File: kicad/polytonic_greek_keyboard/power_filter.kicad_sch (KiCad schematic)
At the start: 6 parts

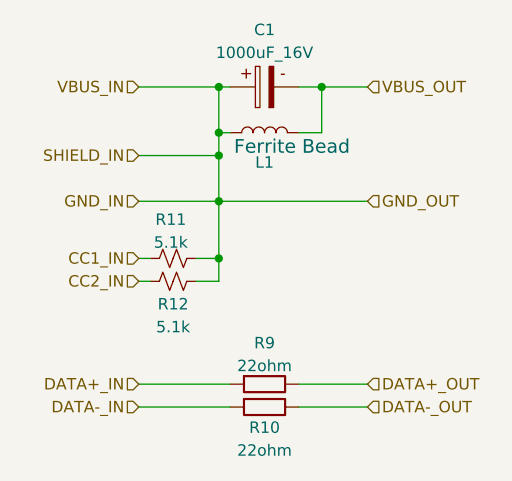
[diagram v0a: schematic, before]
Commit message: [ADD] a more structured approach of the pcb in a way that won't overload the esp32 that is running it
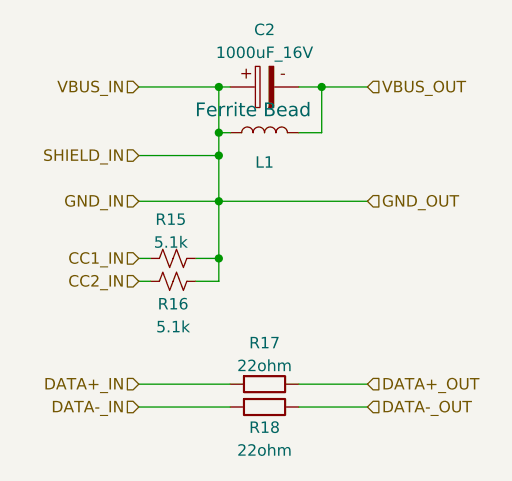
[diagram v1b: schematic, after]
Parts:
- L1: footprint Inductor_SMD:L_6.3x6.3_H3 -> Inductor_SMD:L_0201_0603Metric
- renumbered C1 to C2, R11 to R15, R12 to R16, R9 to R17, R10 to R18
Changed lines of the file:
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@@
 		(on_board yes)
 		(dnp no)
-		(property "Reference" "R10"
+		(property "Reference" "R18"
 			(at 38.1 58.166 0)
 			(effects
@@
 			)
 		)
-		(property "Description" "22Ω, 1/4W Resistor"
+		(property "Description" "20kΩ, 1/4W Resistor"
 			(at 38.1 55.88 0)
 			(effects
@@
 			(project "polytonic_greek_keyboard"
 				(path "/cbe25a1b-6c02-43c2-9ff9-ba274c7cf6a2/603682d4-9510-4466-84d6-fe473c47d1f7"
-					(reference "R10")
+					(reference "R18")
 					(unit 1)
 				)
@@
 		(on_board yes)
 		(dnp no)
-		(property "Reference" "R11"
+		(property "Reference" "R15"
 			(at 27.686 35.052 0)
 			(effects
@@
 			(project ""
 				(path "/cbe25a1b-6c02-43c2-9ff9-ba274c7cf6a2/603682d4-9510-4466-84d6-fe473c47d1f7"
-					(reference "R11")
+					(reference "R15")
 					(unit 1)
 				)
@@
 			)
 		)
-		(property "Footprint" "Inductor_SMD:L_6.3x6.3_H3"
+		(property "Footprint" "Inductor_SMD:L_0201_0603Metric"
 			(at 38.1 25.4 0)
 			(effects
@@
 		)
 		(property "Display" "Ferrite Bead"
-			(at 41.148 26.924 90)
+			(at 36.83 22.86 90)
 			(effects
 				(font
@@
 		(on_board yes)
 		(dnp no)
-		(property "Reference" "C1"
+		(property "Reference" "C2"
 			(at 38.1 13.97 0)
 			(effects
@@
 			(project ""
 				(path "/cbe25a1b-6c02-43c2-9ff9-ba274c7cf6a2/603682d4-9510-4466-84d6-fe473c47d1f7"
-					(reference "C1")
+					(reference "C2")
 					(unit 1)
 				)
@@
 		(on_board yes)
 		(dnp no)
-		(property "Reference" "R12"
+		(property "Reference" "R16"
 			(at 27.94 44.45 0)
 			(effects
@@
 			(project "polytonic_greek_keyboard"
 				(path "/cbe25a1b-6c02-43c2-9ff9-ba274c7cf6a2/603682d4-9510-4466-84d6-fe473c47d1f7"
-					(reference "R12")
+					(reference "R16")
 					(unit 1)
 				)
@@
 		(on_board yes)
 		(dnp no)
-		(property "Reference" "R9"
+		(property "Reference" "R17"
 			(at 38.1 48.768 0)
 			(effects
@@
 			)
 		)
-		(property "Description" "22Ω, 1/4W Resistor"
+		(property "Description" "20kΩ, 1/4W Resistor"
 			(at 38.1 53.34 0)
 			(effects
@@
 			(project ""
 				(path "/cbe25a1b-6c02-43c2-9ff9-ba274c7cf6a2/603682d4-9510-4466-84d6-fe473c47d1f7"
-					(reference "R9")
-					(unit 1)
-				)
+					(reference "R17")
+					(unit 1)
+				)

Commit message: [UPDATE] the board desing, [FIX] connection issues
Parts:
- L1: footprint Inductor_SMD:L_0201_0603Metric -> Inductor_SMD:L_0201_0603Metric_Pad0.64x0.40mm_HandSolder
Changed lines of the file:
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@@
 			)
 		)
-		(property "Footprint" "Inductor_SMD:L_0201_0603Metric"
+		(property "Footprint" "Inductor_SMD:L_0201_0603Metric_Pad0.64x0.40mm_HandSolder"
 			(at 38.1 25.4 0)
 			(effects

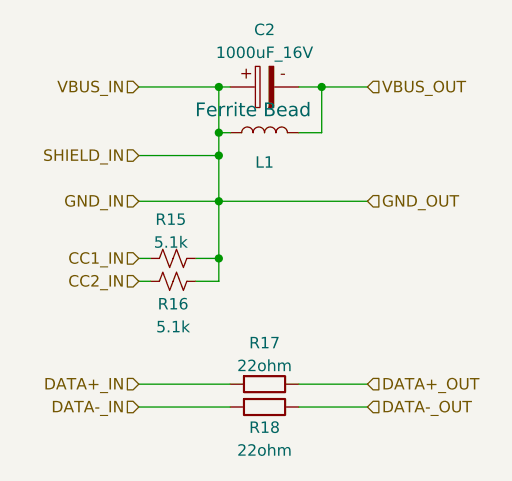
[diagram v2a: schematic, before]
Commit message: [UPDATE] the desing to fit on two separate pcbs
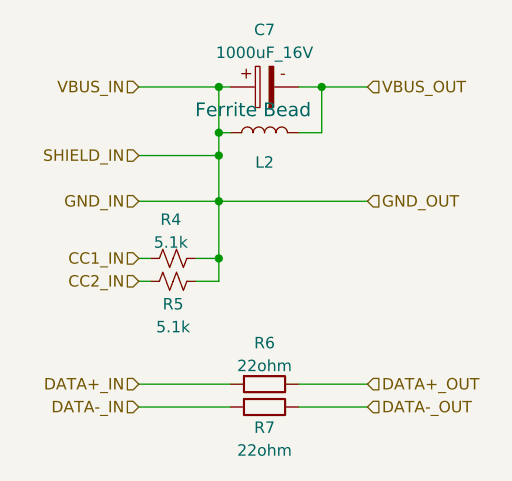
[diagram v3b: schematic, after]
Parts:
- renumbered C2 to C7, L1 to L2, R15 to R4, R16 to R5, R17 to R6, R18 to R7
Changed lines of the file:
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@@
 		(on_board yes)
 		(dnp no)
-		(property "Reference" "R18"
+		(property "Reference" "R7"
 			(at 38.1 58.166 0)
 			(effects
@@
 		(instances
 			(project "polytonic_greek_keyboard"
-				(path "/cbe25a1b-6c02-43c2-9ff9-ba274c7cf6a2/603682d4-9510-4466-84d6-fe473c47d1f7"
-					(reference "R18")
+				(path "/cbe25a1b-6c02-43c2-9ff9-ba274c7cf6a2/8498b325-11fd-4b20-a704-75ec3d8987ef/085bf86b-e0cc-40ae-815c-511e7d27e866"
+					(reference "R7")
 					(unit 1)
 				)
@@
 		(on_board yes)
 		(dnp no)
-		(property "Reference" "R15"
+		(property "Reference" "R4"
 			(at 27.686 35.052 0)
 			(effects
@@
 		)
 		(instances
-			(project ""
-				(path "/cbe25a1b-6c02-43c2-9ff9-ba274c7cf6a2/603682d4-9510-4466-84d6-fe473c47d1f7"
-					(reference "R15")
+			(project "polytonic_greek_keyboard"
+				(path "/cbe25a1b-6c02-43c2-9ff9-ba274c7cf6a2/8498b325-11fd-4b20-a704-75ec3d8987ef/085bf86b-e0cc-40ae-815c-511e7d27e866"
+					(reference "R4")
 					(unit 1)
 				)
@@
 		(on_board yes)
 		(dnp no)
-		(property "Reference" "L1"
+		(property "Reference" "L2"
 			(at 38.1 28.702 90)
 			(effects
@@
 		)
 		(instances
-			(project ""
-				(path "/cbe25a1b-6c02-43c2-9ff9-ba274c7cf6a2/603682d4-9510-4466-84d6-fe473c47d1f7"
-					(reference "L1")
+			(project "polytonic_greek_keyboard"
+				(path "/cbe25a1b-6c02-43c2-9ff9-ba274c7cf6a2/8498b325-11fd-4b20-a704-75ec3d8987ef/085bf86b-e0cc-40ae-815c-511e7d27e866"
+					(reference "L2")
 					(unit 1)
 				)
@@
 		(on_board yes)
 		(dnp no)
-		(property "Reference" "C2"
+		(property "Reference" "C7"
 			(at 38.1 13.97 0)
 			(effects
@@
 		)
 		(instances
-			(project ""
-				(path "/cbe25a1b-6c02-43c2-9ff9-ba274c7cf6a2/603682d4-9510-4466-84d6-fe473c47d1f7"
-					(reference "C2")
+			(project "polytonic_greek_keyboard"
+				(path "/cbe25a1b-6c02-43c2-9ff9-ba274c7cf6a2/8498b325-11fd-4b20-a704-75ec3d8987ef/085bf86b-e0cc-40ae-815c-511e7d27e866"
+					(reference "C7")
 					(unit 1)
 				)
@@
 		(on_board yes)
 		(dnp no)
-		(property "Reference" "R16"
+		(property "Reference" "R5"
 			(at 27.94 44.45 0)
 			(effects
@@
 		(instances
 			(project "polytonic_greek_keyboard"
-				(path "/cbe25a1b-6c02-43c2-9ff9-ba274c7cf6a2/603682d4-9510-4466-84d6-fe473c47d1f7"
-					(reference "R16")
+				(path "/cbe25a1b-6c02-43c2-9ff9-ba274c7cf6a2/8498b325-11fd-4b20-a704-75ec3d8987ef/085bf86b-e0cc-40ae-815c-511e7d27e866"
+					(reference "R5")
 					(unit 1)
 				)
@@
 		(on_board yes)
 		(dnp no)
-		(property "Reference" "R17"
+		(property "Reference" "R6"
 			(at 38.1 48.768 0)
 			(effects
@@
 		)
 		(instances
-			(project ""
-				(path "/cbe25a1b-6c02-43c2-9ff9-ba274c7cf6a2/603682d4-9510-4466-84d6-fe473c47d1f7"
-					(reference "R17")
-					(unit 1)
-				)
+			(project "polytonic_greek_keyboard"
+				(path "/cbe25a1b-6c02-43c2-9ff9-ba274c7cf6a2/8498b325-11fd-4b20-a704-75ec3d8987ef/085bf86b-e0cc-40ae-815c-511e7d27e866"
+					(reference "R6")
+					(unit 1)
+				)

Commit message: [UPDATE] anotation issues
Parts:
- renumbered C7 to C5, R4 to R11, R5 to R12, R6 to R13, R7 to R14
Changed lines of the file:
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@@
 		(on_board yes)
 		(dnp no)
-		(property "Reference" "R7"
+		(property "Reference" "R14"
 			(at 38.1 58.166 0)
 			(effects
@@
 			(project "polytonic_greek_keyboard"
 				(path "/cbe25a1b-6c02-43c2-9ff9-ba274c7cf6a2/8498b325-11fd-4b20-a704-75ec3d8987ef/085bf86b-e0cc-40ae-815c-511e7d27e866"
-					(reference "R7")
+					(reference "R14")
 					(unit 1)
 				)
@@
 		(on_board yes)
 		(dnp no)
-		(property "Reference" "R4"
+		(property "Reference" "R11"
 			(at 27.686 35.052 0)
 			(effects
@@
 			(project "polytonic_greek_keyboard"
 				(path "/cbe25a1b-6c02-43c2-9ff9-ba274c7cf6a2/8498b325-11fd-4b20-a704-75ec3d8987ef/085bf86b-e0cc-40ae-815c-511e7d27e866"
-					(reference "R4")
+					(reference "R11")
 					(unit 1)
 				)
@@
 		(on_board yes)
 		(dnp no)
-		(property "Reference" "C7"
+		(property "Reference" "C5"
 			(at 38.1 13.97 0)
 			(effects
@@
 			(project "polytonic_greek_keyboard"
 				(path "/cbe25a1b-6c02-43c2-9ff9-ba274c7cf6a2/8498b325-11fd-4b20-a704-75ec3d8987ef/085bf86b-e0cc-40ae-815c-511e7d27e866"
-					(reference "C7")
+					(reference "C5")
 					(unit 1)
 				)
@@
 		(on_board yes)
 		(dnp no)
-		(property "Reference" "R5"
+		(property "Reference" "R12"
 			(at 27.94 44.45 0)
 			(effects
@@
 			(project "polytonic_greek_keyboard"
 				(path "/cbe25a1b-6c02-43c2-9ff9-ba274c7cf6a2/8498b325-11fd-4b20-a704-75ec3d8987ef/085bf86b-e0cc-40ae-815c-511e7d27e866"
-					(reference "R5")
+					(reference "R12")
 					(unit 1)
 				)
@@
 		(on_board yes)
 		(dnp no)
-		(property "Reference" "R6"
+		(property "Reference" "R13"
 			(at 38.1 48.768 0)
 			(effects
@@
 			(project "polytonic_greek_keyboard"
 				(path "/cbe25a1b-6c02-43c2-9ff9-ba274c7cf6a2/8498b325-11fd-4b20-a704-75ec3d8987ef/085bf86b-e0cc-40ae-815c-511e7d27e866"
-					(reference "R6")
-					(unit 1)
-				)
+					(reference "R13")
+					(unit 1)
+				)

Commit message: [UPDATE] the final merged version of the schematic before splitting into two separate kicad projects
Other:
- company: (none) -> Henry's Software House
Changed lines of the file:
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@@
 	(generator_version "9.0")
 	(paper "A4")
+	(title_block
+		(rev "1 - do not edit connector pin layout.")
+		(company "Henry's Software House")
+	)
 	(junction
 		(at 33.02 33.02)
